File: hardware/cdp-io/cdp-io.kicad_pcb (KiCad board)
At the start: 2 copper layers, 99.1 x 99.1 mm, 18 parts, among them J1 Conn_01x26_Pin, U1 74LS573, U2 74LS573, U3 74LS573, U4 74LS573, U5 74LS573, U6 74LS573, U7 74LS00

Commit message: The controller is finished. U7 is changed to a hex inverter.
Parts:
- added C10: 100n, Capacitor_THT:C_Disc_D3.0mm_W1.6mm_P2.50mm, F.Cu at (18.9, 35.9)
- added C7: 100n, Capacitor_THT:C_Disc_D3.0mm_W1.6mm_P2.50mm, F.Cu at (18.9, 26.5)
- added C8: 100n, Capacitor_THT:C_Disc_D3.0mm_W1.6mm_P2.50mm, F.Cu at (18.9, 29.6)
- added C9: 100n, Capacitor_THT:C_Disc_D3.0mm_W1.6mm_P2.50mm, F.Cu at (18.9, 32.8)
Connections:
- J1 pad 1: unconnected-(J1-Pin_1-Pad1) -> PORTA0
- J1 pad 10: unconnected-(J1-Pin_10-Pad10) -> PORTB0
- J1 pad 11: unconnected-(J1-Pin_11-Pad11) -> PORTB1
- J1 pad 12: unconnected-(J1-Pin_12-Pad12) -> PORTB2
- J1 pad 13: unconnected-(J1-Pin_13-Pad13) -> PORTB3
- J1 pad 14: unconnected-(J1-Pin_14-Pad14) -> PORTB4
- J1 pad 15: unconnected-(J1-Pin_15-Pad15) -> PORTB5
- J1 pad 16: unconnected-(J1-Pin_16-Pad16) -> PORTB6
- J1 pad 17: unconnected-(J1-Pin_17-Pad17) -> PORTB7
- J1 pad 18: unconnected-(J1-Pin_18-Pad18) -> GND
- J1 pad 19: unconnected-(J1-Pin_19-Pad19) -> PORTC0
- J1 pad 2: unconnected-(J1-Pin_2-Pad2) -> PORTA1
- J1 pad 20: unconnected-(J1-Pin_20-Pad20) -> PORTC1
- J1 pad 21: unconnected-(J1-Pin_21-Pad21) -> PORTC2
- J1 pad 22: unconnected-(J1-Pin_22-Pad22) -> PORTC3
- J1 pad 23: unconnected-(J1-Pin_23-Pad23) -> PORTC4
- J1 pad 24: unconnected-(J1-Pin_24-Pad24) -> PORTC5
- J1 pad 25: unconnected-(J1-Pin_25-Pad25) -> PORTC6
- J1 pad 26: unconnected-(J1-Pin_26-Pad26) -> PORTC7
- J1 pad 3: unconnected-(J1-Pin_3-Pad3) -> PORTA2
- J1 pad 4: unconnected-(J1-Pin_4-Pad4) -> PORTA3
- J1 pad 5: unconnected-(J1-Pin_5-Pad5) -> PORTA4
- J1 pad 6: unconnected-(J1-Pin_6-Pad6) -> PORTA5
- J1 pad 7: unconnected-(J1-Pin_7-Pad7) -> PORTA6
- J1 pad 8: unconnected-(J1-Pin_8-Pad8) -> PORTA7
- J1 pad 9: unconnected-(J1-Pin_9-Pad9) -> GND

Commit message: Changed the layout a bit, started to work on the PCB.
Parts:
- added U10: 74LS175, Package_DIP:DIP-16_W7.62mm_Socket, F.Cu at (139.7, 104.1)
- added U8: 74LS138, Package_DIP:DIP-16_W7.62mm_Socket, F.Cu at (127.0, 38.1)
- added U9: 74LS138, Package_DIP:DIP-16_W7.62mm_Socket, F.Cu at (139.7, 38.1)
- U7: value 74LS00 -> 74LS14
- moved C10 143.7 mm to (147.3, 100.3), turned to 180 degrees
- moved C7 138.2 mm to (147.3, 77.5), turned to 180 degrees
- moved C9 128.5 mm to (147.3, 34.3), turned to 180 degrees
- moved C8 115.9 mm to (134.6, 34.3), turned to 180 degrees
- moved U7 43.2 mm to (139.7, 81.3)
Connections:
- U7 pad 10: ~{PORTC WRITE} -> Net-(U10-Cp)
- U7 pad 11: (no net) -> ~{CTRL WRITE}
- U7 pad 12: (no net) -> unconnected-(U7-Pad12)
- U7 pad 13: (no net) -> unconnected-(U7-Pad13)
- U7 pad 14: (no net) -> VCC
- U7 pad 2: ~{PORTA WRITE} -> Net-(U1-Load)
- U7 pad 3: Net-(U1-Load) -> ~{PORTB WRITE}
- U7 pad 4: ~{PORTB WRITE} -> Net-(U3-Load)
- U7 pad 5: ~{PORTB WRITE} -> ~{PORTC WRITE}
- U7 pad 6: Net-(U3-Load) -> Net-(U5-Load)
- U7 pad 7: (no net) -> GND
- U7 pad 8: Net-(U5-Load) -> Net-(U8-E1)
- U7 pad 9: ~{PORTC WRITE} -> TPB
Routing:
- net Net-(U5-Load): track 90.5 -> 3.81 mm
- net ~{PORTC READ}: track 0.00 -> 71.2 mm, vias 0 -> 1
- net Net-(U3-Load): track 70.2 -> 2.54 mm
- net ~{PORTB READ}: track 0.00 -> 44.8 mm, vias 0 -> 1
- net Net-(U1-Load): track 47.3 -> 3.07 mm
- net ~{PORTC OUTPUT}: track 0.00 -> 37.1 mm
- net ~{PORTA READ}: track 0.00 -> 32.1 mm, vias 0 -> 1
- net Net-(U8-E1): track 0.00 -> 13.8 mm
- net N2: track 0.00 -> 13.8 mm
- net N1: track 0.00 -> 13.8 mm
- net N0: track 0.00 -> 13.8 mm
- net D2: track 151.7 -> 163.7 mm
- net ~{PORTC WRITE}: track 2.54 -> 0.00 mm
- net ~{PORTB WRITE}: track 2.54 -> 0.00 mm
- net ~{PORTA WRITE}: track 2.54 -> 0.00 mm

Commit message: Changed the schematic a bit.
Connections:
- U10 pad 11: ~{PORTC OUTPUT} -> ~{PORTB OUTPUT}
- U10 pad 12: D2 -> D1
- U10 pad 13: D3 -> D2
- U10 pad 14: unconnected-(U10-~{Q3}-Pad14) -> ~{PORTC OUTPUT}
- U10 pad 5: D1 -> D3
- U10 pad 6: ~{PORTB OUTPUT} -> unconnected-(U10-~{Q1}-Pad6)
- U7 pad 1: ~{PORTA WRITE} -> unconnected-(U7-Pad1)
- U7 pad 10: Net-(U10-Cp) -> Net-(U3-Load)
- U7 pad 11: ~{CTRL WRITE} -> ~{PORTB WRITE}
- U7 pad 12: unconnected-(U7-Pad12) -> Net-(U1-Load)
- U7 pad 13: unconnected-(U7-Pad13) -> ~{PORTA WRITE}
- U7 pad 2: Net-(U1-Load) -> unconnected-(U7-Pad2)
- U7 pad 3: ~{PORTB WRITE} -> ~{CTRL WRITE}
- U7 pad 4: Net-(U3-Load) -> Net-(U10-Cp)
- U7 pad 5: ~{PORTC WRITE} -> TPB
- U7 pad 6: Net-(U5-Load) -> Net-(U8-E1)
- U7 pad 8: Net-(U8-E1) -> Net-(U5-Load)
- U7 pad 9: TPB -> ~{PORTC WRITE}
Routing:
- net ~{PORTB OUTPUT}: track 0.00 -> 66.9 mm
- net Net-(U1-Load): track 3.07 -> 46.6 mm, vias 0 -> 3
- net Net-(U5-Load): track 3.81 -> 44.8 mm, vias 0 -> 2
- net ~{PORTA OUTPUT}: track 0.00 -> 24.7 mm
- net Net-(U3-Load): track 2.54 -> 22.6 mm, vias 0 -> 1
- net D0: track 159.4 -> 176.7 mm
- net D3: track 147.9 -> 164.0 mm
- net D1: track 155.6 -> 168.0 mm
- net ~{PORTC OUTPUT}: track 37.1 -> 27.0 mm
- net D2: track 163.7 -> 160.4 mm, vias 2 -> 3
- net D6: track 136.5 -> 135.8 mm
- net D4: track 144.1 -> 143.4 mm
- net D7: track 132.7 -> 132.0 mm
- net D5: track 140.3 -> 139.6 mm

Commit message: A really small progress.
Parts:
- added J2: Conn_02x20_Odd_Even, Connector_IDC:IDC-Header_2x20_P2.54mm_Vertical, F.Cu at (106.7, 54.6)
- moved U9 68.2 mm to (122.6, 104.1)
- moved U8 66.6 mm to (135.3, 104.1)
- moved C10 66.2 mm to (142.9, 34.3)
- moved C8 66.2 mm to (130.2, 100.3)
- moved C9 66.2 mm to (142.9, 100.3)
- moved U10 66.2 mm to (135.3, 38.1)
- moved U7 17.1 mm to (135.3, 64.8)
- moved C7 17.1 mm to (142.9, 61.0)
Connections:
- net ~{MRW} renamed ~{MWR}
- U10 pad 13: D2 -> D0
- U10 pad 14: ~{PORTC OUTPUT} -> ~{PORTA OUTPUT}
- U10 pad 3: ~{PORTA OUTPUT} -> unconnected-(U10-~{Q0}-Pad3)
- U10 pad 4: D0 -> D3
- U10 pad 5: D3 -> D2
- U10 pad 6: unconnected-(U10-~{Q1}-Pad6) -> ~{PORTC OUTPUT}
- U7 pad 1: unconnected-(U7-Pad1) -> ~{CTRL WRITE}
- U7 pad 2: unconnected-(U7-Pad2) -> Net-(U10-Cp)
- U7 pad 3: ~{CTRL WRITE} -> unconnected-(U7-Pad3)
- U7 pad 4: Net-(U10-Cp) -> unconnected-(U7-Pad4)
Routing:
- net ~{PORTA READ}: track 32.1 -> 114.1 mm
- net ~{PORTC OUTPUT}: track 27.0 -> 71.3 mm, vias 0 -> 1
- net ~{PORTB READ}: track 44.8 -> 85.1 mm
- net ~{PORTB OUTPUT}: track 66.9 -> 34.7 mm, vias 0 -> 1
- net ~{MRD}: track 0.00 -> 29.5 mm
- net VCC: track 91.4 -> 120.4 mm
- net N2: track 13.8 -> 41.4 mm, vias 0 -> 1
- net ~{MWR}: track 0.00 -> 25.2 mm, vias 0 -> 2
- net N1: track 13.8 -> 36.3 mm, vias 0 -> 1
- net Net-(U5-Load): track 44.8 -> 66.9 mm, vias 2 -> 0
- net ~{CTRL WRITE}: track 0.00 -> 20.6 mm, vias 0 -> 1
- net Net-(U3-Load): track 22.6 -> 41.1 mm
- net Net-(U10-Cp): track 0.00 -> 17.6 mm
- net N0: track 13.8 -> 31.2 mm
- net ~{PORTB WRITE}: track 0.00 -> 15.0 mm, vias 0 -> 1
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
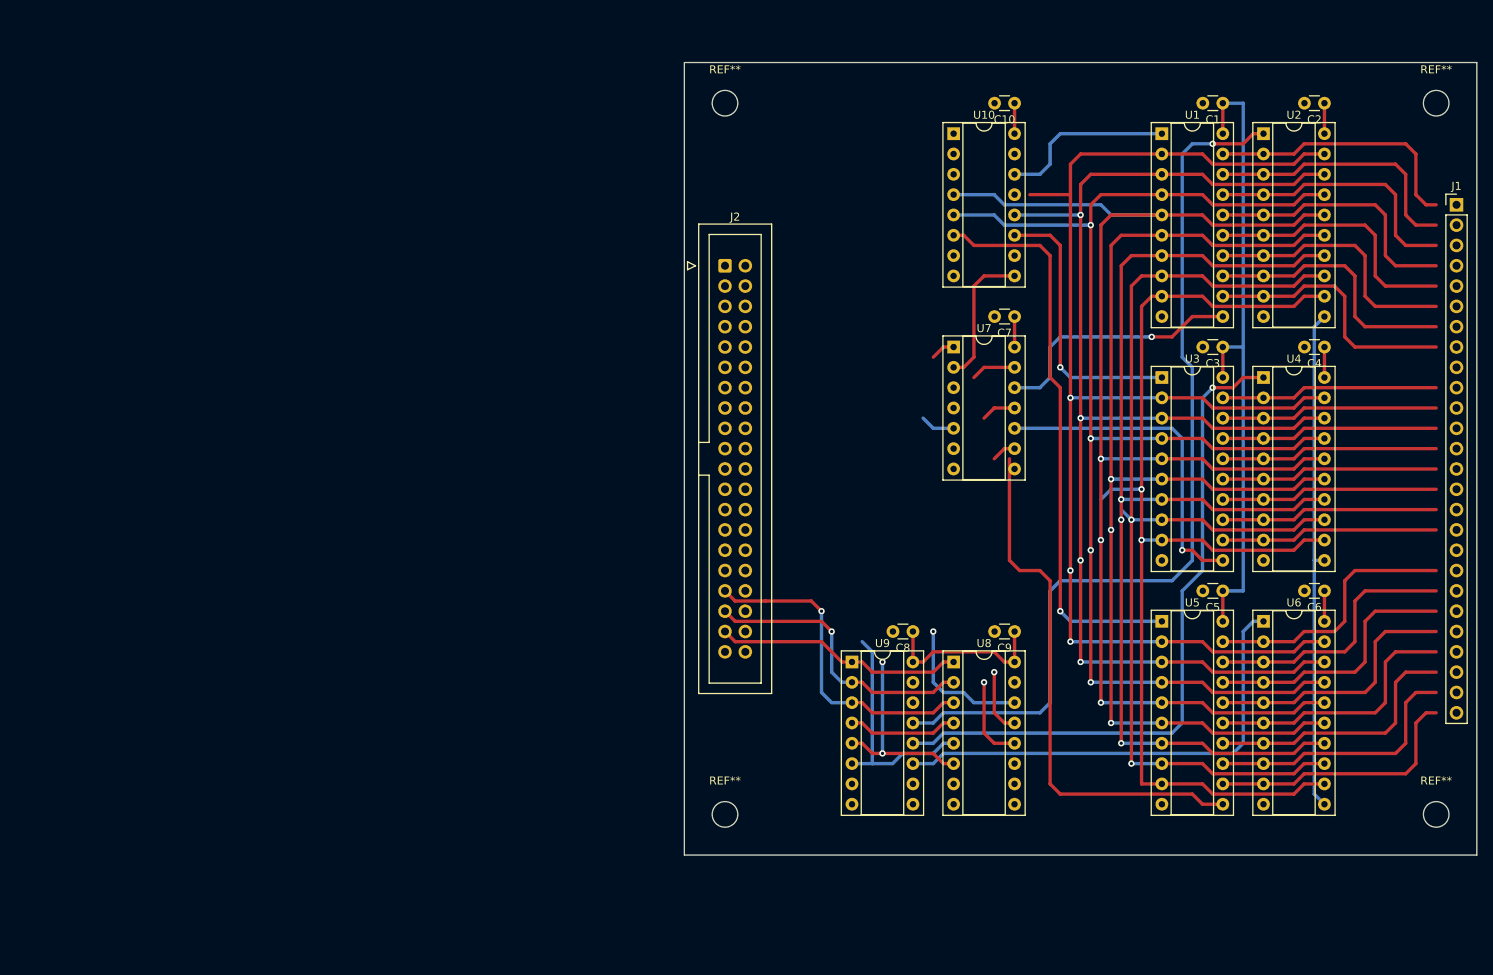
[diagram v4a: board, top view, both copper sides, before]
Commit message: Renamed a few net, and changed the schematic a bit. The PCB is ready!
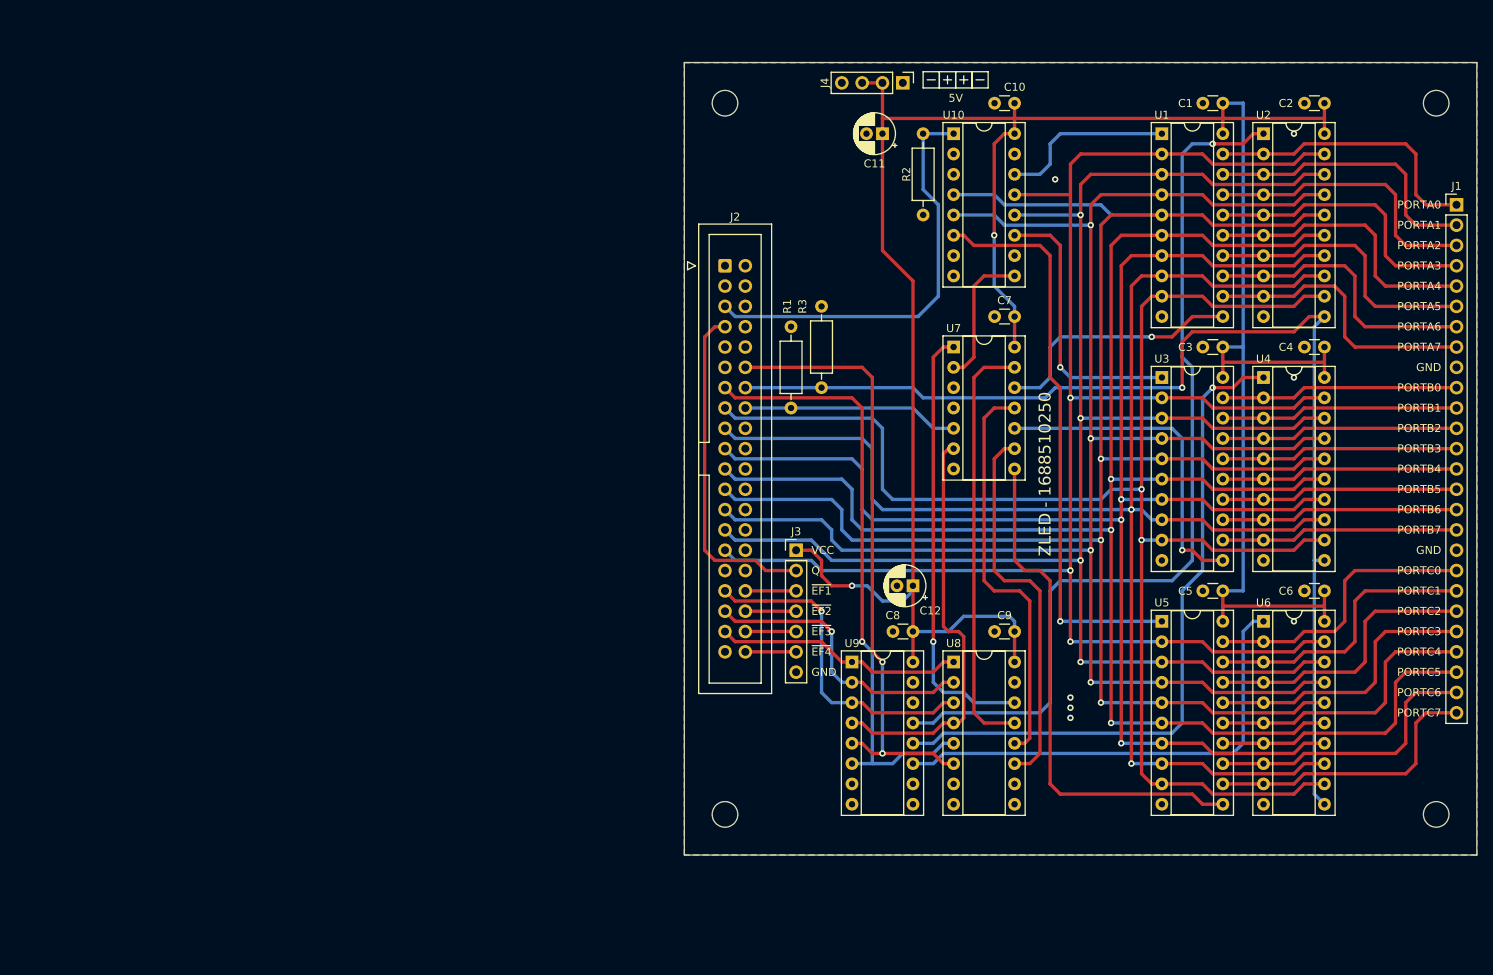
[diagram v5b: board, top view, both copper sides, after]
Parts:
- added C11: 22uF, Capacitor_THT:CP_Radial_D5.0mm_P2.00mm, F.Cu at (126.4, 38.1)
- added C12: 22uF, Capacitor_THT:CP_Radial_D5.0mm_P2.00mm, F.Cu at (130.2, 94.6)
- added J3: Conn_01x07_Pin, Connector_PinHeader_2.54mm:PinHeader_1x07_P2.54mm_Vertical, F.Cu at (115.6, 90.2)
- added J4: Conn_01x04_Pin, Connector_PinHeader_2.54mm:PinHeader_1x04_P2.54mm_Vertical, F.Cu at (128.9, 31.8)
- added R1: 47k, Resistor_THT:R_Axial_DIN0207_L6.3mm_D2.5mm_P10.16mm_Horizontal, F.Cu at (114.9, 72.4)
- added R2: 47k, Resistor_THT:R_Axial_DIN0207_L6.3mm_D2.5mm_P10.16mm_Horizontal, F.Cu at (131.4, 38.1)
- added R3: 47k, Resistor_THT:R_Axial_DIN0207_L6.3mm_D2.5mm_P10.16mm_Horizontal, F.Cu at (118.7, 69.8)
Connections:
- J2 pad 2: VCC -> unconnected-(J2-Pin_2-Pad2)
- J2 pad 31: VCC -> unconnected-(J2-Pin_31-Pad31)
- U1 pad 12: OUTA7 -> PORTA7
- U1 pad 13: OUTA6 -> PORTA6
- U1 pad 14: OUTA5 -> PORTA5
- U1 pad 15: OUTA4 -> PORTA4
- U1 pad 16: OUTA3 -> PORTA3
- U1 pad 17: OUTA2 -> PORTA2
- U1 pad 18: OUTA1 -> PORTA1
- U1 pad 19: OUTA0 -> PORTA0
- U10 pad 1: ~{RESET} -> ~{CLEAR}
- U2 pad 2: OUTA0 -> PORTA0
- U2 pad 3: OUTA1 -> PORTA1
- U2 pad 4: OUTA2 -> PORTA2
- U2 pad 5: OUTA3 -> PORTA3
- U2 pad 6: OUTA4 -> PORTA4
- U2 pad 7: OUTA5 -> PORTA5
- U2 pad 8: OUTA6 -> PORTA6
- U2 pad 9: OUTA7 -> PORTA7
- U3 pad 12: OUTB7 -> PORTB7
- U3 pad 13: OUTB6 -> PORTB6
- U3 pad 14: OUTB5 -> PORTB5
- U3 pad 15: OUTB4 -> PORTB4
- U3 pad 16: OUTB3 -> PORTB3
- U3 pad 17: OUTB2 -> PORTB2
- U3 pad 18: OUTB1 -> PORTB1
- U3 pad 19: OUTB0 -> PORTB0
- U4 pad 2: OUTB0 -> PORTB0
- U4 pad 3: OUTB1 -> PORTB1
- U4 pad 4: OUTB2 -> PORTB2
- U4 pad 5: OUTB3 -> PORTB3
- U4 pad 6: OUTB4 -> PORTB4
- U4 pad 7: OUTB5 -> PORTB5
- U4 pad 8: OUTB6 -> PORTB6
- U4 pad 9: OUTB7 -> PORTB7
- U5 pad 12: OUTC7 -> PORTC7
- U5 pad 13: OUTC6 -> PORTC6
- U5 pad 14: OUTC5 -> PORTC5
- U5 pad 15: OUTC4 -> PORTC4
- U5 pad 16: OUTC3 -> PORTC3
- U5 pad 17: OUTC2 -> PORTC2
- U5 pad 18: OUTC1 -> PORTC1
- U5 pad 19: OUTC0 -> PORTC0
- U6 pad 2: OUTC0 -> PORTC0
- U6 pad 3: OUTC1 -> PORTC1
- U6 pad 4: OUTC2 -> PORTC2
- U6 pad 5: OUTC3 -> PORTC3
- U6 pad 6: OUTC4 -> PORTC4
- U6 pad 7: OUTC5 -> PORTC5
- U6 pad 8: OUTC6 -> PORTC6
- U6 pad 9: OUTC7 -> PORTC7
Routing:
- net VCC: track 120.4 -> 320.3 mm, vias 0 -> 2
- net TPA: track 63.3 -> 143.8 mm, vias 0 -> 1
- net D6: track 137.6 -> 195.0 mm
- net D5: track 139.6 -> 195.8 mm
- net D7: track 137.6 -> 193.0 mm
- net D4: track 143.4 -> 197.0 mm
- net ~{CLEAR}: track 0.00 -> 53.2 mm
- net ~{MWR}: track 25.2 -> 77.7 mm
- net D3: track 174.3 -> 225.4 mm
- net D2: track 168.7 -> 217.2 mm
- net ~{MRD}: track 29.5 -> 76.9 mm, vias 0 -> 1
- net D0: track 163.7 -> 209.8 mm
- net D1: track 163.1 -> 209.1 mm
- net ~{PORTC WRITE}: track 3.07 -> 47.8 mm
- net Q: track 0.00 -> 42.2 mm
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- added copper zone on B.Cu, net GND
- added copper zone on F.Cu, net GND
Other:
- board text added: "5V"
- board text added: "GND"
- board text added: "PORTA0"
- board text added: "PORTA1"
- board text added: "PORTA2"
- board text added: "PORTA3"
- board text added: "PORTA4"
- board text added: "PORTA5"
- board text added: "PORTA6"
- board text added: "PORTA7"
- board text added: "PORTB0"
- board text added: "PORTB1"
- board text added: "PORTB2"
- board text added: "PORTB3"
- board text added: "PORTB4"
- board text added: "PORTB5"
- board text added: "PORTB6"
- board text added: "PORTB7"
- board text added: "PORTC0"
- board text added: "PORTC1"
- board text added: "PORTC2"
- board text added: "PORTC3"
- board text added: "PORTC4"
- board text added: "PORTC5"
- board text added: "PORTC6"
- board text added: "PORTC7"
- board text added: "Q"
- board text added: "VCC"
- board text added: "ZLED - 1688510250"
- board text added: "~{EF1}"
- board text added: "~{EF2}"
- board text added: "~{EF3}"
- board text added: "~{EF4}"

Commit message: The final version of the IO board. Gerber files added.
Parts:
- moved C12 13.1 mm to (128.4, 107.6)
- moved C4 13.1 mm to (179.8, 77.7)
- moved C8 13.1 mm to (128.4, 113.3)
- moved R3 13.1 mm to (117.0, 82.8)
- moved REF** 13.1 mm to (104.9, 136.1)
- moved REF** 13.1 mm to (193.8, 136.1)
- moved U4 13.1 mm to (172.2, 81.5)
- moved C3 13.1 mm to (167.1, 77.7)
- moved C9 13.1 mm to (141.1, 113.3)
- moved U3 13.1 mm to (159.5, 81.5)
- moved U7 13.1 mm to (133.5, 77.7)
- moved C2 13.1 mm to (179.8, 47.2)
- moved J4 13.1 mm to (127.1, 44.7)
- moved REF** 13.1 mm to (193.8, 47.2)
- moved REF** 13.1 mm to (104.9, 47.2)
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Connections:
- U7 pad 3: unconnected-(U7-Pad3) -> GND

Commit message: IC names fixed. PCB is updated. Gerber files are still ok.
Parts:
- U1, U2, U3, U4, U5, U6: value 74LS573 -> 74HC573
- U10: value 74LS175 -> 74HC175
- U7: value 74LS14 -> 74HC14
- U8, U9: value 74LS138 -> 74HC138
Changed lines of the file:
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@@
         (effects (font (size 1 1) (thickness 0.15)))
     )
-    (fp_text value "74LS573" (at 3.81 25.19) (layer "F.Fab")
+    (fp_text value "74HC573" (at 3.81 25.19) (layer "F.Fab")
         (effects (font (size 1 1) (thickness 0.15)))
     )
@@
         (effects (font (size 1 1) (thickness 0.15)))
     )
-    (fp_text value "74LS573" (at 3.81 25.19) (layer "F.Fab")
+    (fp_text value "74HC573" (at 3.81 25.19) (layer "F.Fab")
         (effects (font (size 1 1) (thickness 0.15)))
     )
@@
         (effects (font (size 1 1) (thickness 0.15)))
     )
-    (fp_text value "74LS573" (at 3.81 25.19) (layer "F.Fab")
+    (fp_text value "74HC573" (at 3.81 25.19) (layer "F.Fab")
         (effects (font (size 1 1) (thickness 0.15)))
     )
@@
         (effects (font (size 1 1) (thickness 0.15)))
     )
-    (fp_text value "74LS138" (at 3.81 20.11) (layer "F.Fab")
+    (fp_text value "74HC138" (at 3.81 20.11) (layer "F.Fab")
         (effects (font (size 1 1) (thickness 0.15)))
     )
@@
         (effects (font (size 1 1) (thickness 0.15)))
     )
-    (fp_text value "74LS14" (at 3.81 17.57) (layer "F.Fab")
+    (fp_text value "74HC14" (at 3.81 17.57) (layer "F.Fab")
         (effects (font (size 1 1) (thickness 0.15)))
     )
@@
         (effects (font (size 1 1) (thickness 0.15)))
     )
-    (fp_text value "74LS175" (at 3.81 20.11) (layer "F.Fab")
+    (fp_text value "74HC175" (at 3.81 20.11) (layer "F.Fab")
         (effects (font (size 1 1) (thickness 0.15)))
     )
@@
         (effects (font (size 1 1) (thickness 0.15)))
     )
-    (fp_text value "74LS573" (at 3.81 25.19) (layer "F.Fab")
+    (fp_text value "74HC573" (at 3.81 25.19) (layer "F.Fab")
         (effects (font (size 1 1) (thickness 0.15)))
     )
@@
         (effects (font (size 1 1) (thickness 0.15)))
     )
-    (fp_text value "74LS573" (at 3.81 25.19) (layer "F.Fab")
+    (fp_text value "74HC573" (at 3.81 25.19) (layer "F.Fab")
         (effects (font (size 1 1) (thickness 0.15)))
     )
@@
         (effects (font (size 1 1) (thickness 0.15)))
     )
-    (fp_text value "74LS138" (at 3.81 20.11) (layer "F.Fab")
+    (fp_text value "74HC138" (at 3.81 20.11) (layer "F.Fab")
         (effects (font (size 1 1) (thickness 0.15)))
     )
@@
         (effects (font (size 1 1) (thickness 0.15)))
     )
-    (fp_text value "74LS573" (at 3.81 25.19) (layer "F.Fab")
-        (effects (font (size 1 1) (thickness 0.15)))
-    )
+    (fp_text value "74HC573" (at 3.81 25.19) (layer "F.Fab")
+        (effects (font (size 1 1) (thickness 0.15)))
+    )
